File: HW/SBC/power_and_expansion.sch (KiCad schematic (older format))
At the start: 13 parts, among them J4 POWER IN, J5 Expansion Port, U11 LM7805

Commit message: Connected all relevant I/O select signals to expansion port.
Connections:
- net labels added: ~7FAX
- wire segments 71 -> 93
- no-connect marks 9 -> 8
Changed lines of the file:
@@
 	2425 2275 2425 2500
 Wire Wire Line
-	1900 2500 5625 2500
+	1900 2500 2425 2500
+Wire Wire Line
+	2425 2500 2825 2500
+Wire Wire Line
+	2825 2500 3225 2500
+Wire Wire Line
+	3225 2500 3550 2500
+Wire Wire Line
+	3550 2500 3800 2500
+Wire Wire Line
+	3800 2500 4050 2500
+Wire Wire Line
+	4050 2500 4300 2500
+Wire Wire Line
+	4300 2500 4550 2500
+Wire Wire Line
+	4550 2500 4800 2500
+Wire Wire Line
+	4800 2500 5050 2500
+Wire Wire Line
+	5050 2500 5300 2500
+Wire Wire Line
+	5300 2500 5625 2500
 Wire Wire Line
 	3225 2500 3225 2275
@@
 	1900 2125 1900 2500
 Wire Wire Line
-	3225 1650 5625 1650
+	3225 1650 3550 1650
+Wire Wire Line
+	3550 1650 3800 1650
+Wire Wire Line
+	3800 1650 4050 1650
+Wire Wire Line
+	4050 1650 4300 1650
+Wire Wire Line
+	4300 1650 4550 1650
+Wire Wire Line
+	4550 1650 4800 1650
+Wire Wire Line
+	4800 1650 5050 1650
+Wire Wire Line
+	5050 1650 5300 1650
+Wire Wire Line
+	5300 1650 5625 1650
 Wire Wire Line
 	3550 1750 3550 1650
@@
 	3350 3725 3350 3500
 Wire Wire Line
-	3350 3500 3850 3500
+	3350 3500 3600 3500
+Wire Wire Line
+	3600 3500 3850 3500
 Wire Wire Line
 	3850 3500 3850 3725
@@
 	3350 6125 3350 6325
 Wire Wire Line
-	3350 6325 3850 6325
+	3350 6325 3600 6325
+Wire Wire Line
+	3600 6325 3850 6325
 Wire Wire Line
 	3850 6325 3850 6125
@@
 Wire Wire Line
 	4250 6025 3850 5725
-NoConn ~ 3850 5825
 NoConn ~ 3850 5925
 NoConn ~ 3850 6025
@@
 	1    0    0    -1
 $EndComp
+Text GLabel 4250 6175 2    60   Input ~ 0
+~7FAX
+Wire Wire Line
+	4250 6175 3850 5825
 $EndSCHEMATC

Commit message: New MB design. Includes RTC. New IDE design.
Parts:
- removed U11: LM7805, TO_SOT_Packages_THT:TO-220_Vertical, symbol LM7805
- added U11: LM7805CT, TO_SOT_Packages_THT:TO-220_Vertical, symbol LM7805CT
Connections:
- wire segments 93 -> 72
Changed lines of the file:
@@
 $EndDescr
-$Comp
-L LM7805 U11
-U 1 1 58D5E978
-P 2825 1700
-F 0 "U11" H 2975 1504 50  0000 C CNN
-F 1 "LM7805" H 2825 1900 50  0000 C CNN
-F 2 "TO_SOT_Packages_THT:TO-220_Vertical" H 2825 1700 50  0001 C CNN
-F 3 "" H 2825 1700 50  0001 C CNN
-	1    2825 1700
-	1    0    0    -1
-$EndComp
 $Comp
 L CP1_Small C7
@@
 	2425 2275 2425 2500
 Wire Wire Line
-	1900 2500 2425 2500
-Wire Wire Line
-	2425 2500 2825 2500
-Wire Wire Line
-	2825 2500 3225 2500
-Wire Wire Line
-	3225 2500 3550 2500
-Wire Wire Line
-	3550 2500 3800 2500
-Wire Wire Line
-	3800 2500 4050 2500
-Wire Wire Line
-	4050 2500 4300 2500
-Wire Wire Line
-	4300 2500 4550 2500
-Wire Wire Line
-	4550 2500 4800 2500
-Wire Wire Line
-	4800 2500 5050 2500
-Wire Wire Line
-	5050 2500 5300 2500
-Wire Wire Line
-	5300 2500 5625 2500
+	1900 2500 5625 2500
 Wire Wire Line
 	3225 2500 3225 2275
@@
 	1900 2125 1900 2500
 Wire Wire Line
-	3225 1650 3550 1650
-Wire Wire Line
-	3550 1650 3800 1650
-Wire Wire Line
-	3800 1650 4050 1650
-Wire Wire Line
-	4050 1650 4300 1650
-Wire Wire Line
-	4300 1650 4550 1650
-Wire Wire Line
-	4550 1650 4800 1650
-Wire Wire Line
-	4800 1650 5050 1650
-Wire Wire Line
-	5050 1650 5300 1650
-Wire Wire Line
-	5300 1650 5625 1650
+	3225 1650 5625 1650
 Wire Wire Line
 	3550 1750 3550 1650
@@
 	3350 3725 3350 3500
 Wire Wire Line
-	3350 3500 3600 3500
-Wire Wire Line
-	3600 3500 3850 3500
+	3350 3500 3850 3500
 Wire Wire Line
 	3850 3500 3850 3725
@@
 	3350 6125 3350 6325
 Wire Wire Line
-	3350 6325 3600 6325
-Wire Wire Line
-	3600 6325 3850 6325
+	3350 6325 3850 6325
 Wire Wire Line
 	3850 6325 3850 6125
@@
 Wire Wire Line
 	4250 6175 3850 5825
+$Comp
+L LM7805CT U11
+U 1 1 58E10ED4
+P 2825 1700
+F 0 "U11" H 2625 1900 50  0000 C CNN
+F 1 "LM7805CT" H 2825 1900 50  0000 L CNN
+F 2 "TO_SOT_Packages_THT:TO-220_Vertical" H 2825 1800 50  0001 C CIN
+F 3 "" H 2825 1700 50  0001 C CNN
+	1    2825 1700
+	1    0    0    -1
+$EndComp
 $EndSCHEMATC

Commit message: Updates to pcb and monitor.
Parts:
- J5: footprint Pin_Headers:Pin_Header_Straight_2x25_Pitch2.54mm -> Connect:IDC_Header_Straight_50pins
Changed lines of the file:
@@
 $EndComp
 $Comp
-L VCC #PWR028
+L VCC #PWR029
 U 1 1 58D5EE10
 P 5625 1650
-F 0 "#PWR028" H 5625 1500 50  0001 C CNN
+F 0 "#PWR029" H 5625 1500 50  0001 C CNN
 F 1 "VCC" H 5625 1800 50  0000 C CNN
 F 2 "" H 5625 1650 50  0001 C CNN
@@
 F 0 "J5" H 3600 6225 50  0000 C CNN
 F 1 "Expansion Port" V 3600 4925 50  0000 C CNN
-F 2 "Pin_Headers:Pin_Header_Straight_2x25_Pitch2.54mm" H 3600 4175 50  0001 C CNN
+F 2 "Connect:IDC_Header_Straight_50pins" H 3600 4175 50  0001 C CNN
 F 3 "" H 3600 4175 50  0001 C CNN
 	1    3600 4925
@@
 	5300 1950 5300 2500
 $Comp
-L VCC #PWR029
+L VCC #PWR030
 U 1 1 58D7686C
 P 3600 3500
-F 0 "#PWR029" H 3600 3350 50  0001 C CNN
+F 0 "#PWR030" H 3600 3350 50  0001 C CNN
 F 1 "VCC" H 3600 3650 50  0000 C CNN
 F 2 "" H 3600 3500 50  0001 C CNN
@@
 Connection ~ 3600 3500
 $Comp
-L GND #PWR030
+L GND #PWR031
 U 1 1 58D76B4A
 P 3600 6325
-F 0 "#PWR030" H 3600 6075 50  0001 C CNN
+F 0 "#PWR031" H 3600 6075 50  0001 C CNN
 F 1 "GND" H 3600 6175 50  0000 C CNN
 F 2 "" H 3600 6325 50  0001 C CNN
@@
 Connection ~ 5300 2500
 $Comp
-L GND #PWR031
+L GND #PWR032
 U 1 1 58D85868
 P 5625 2500
-F 0 "#PWR031" H 5625 2250 50  0001 C CNN
+F 0 "#PWR032" H 5625 2250 50  0001 C CNN
 F 1 "GND" H 5625 2350 50  0000 C CNN
 F 2 "" H 5625 2500 50  0001 C CNN

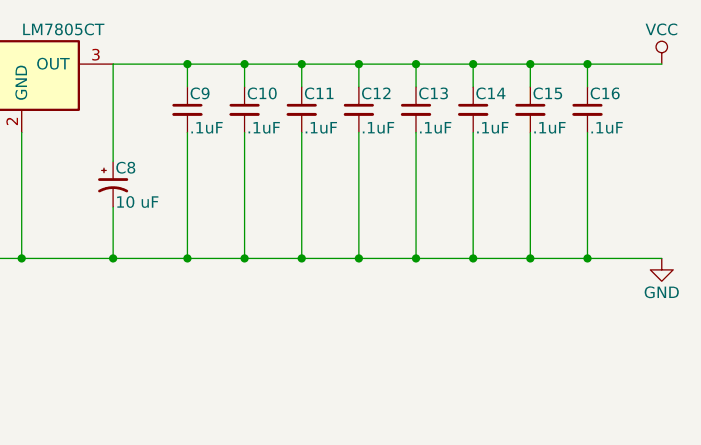
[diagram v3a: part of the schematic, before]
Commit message: Move dicoupling capacitators as close the chips as possible.
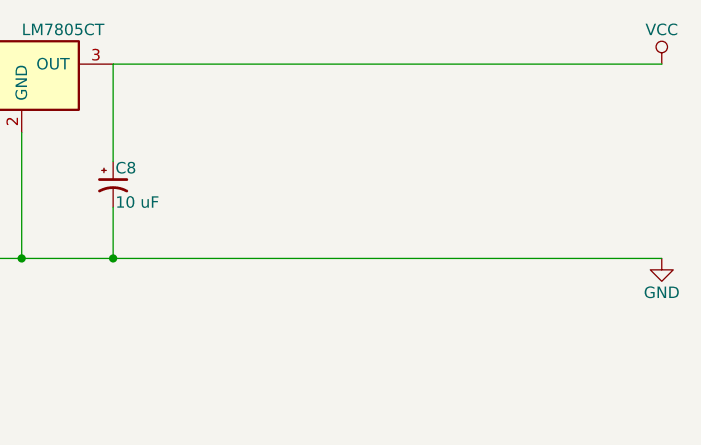
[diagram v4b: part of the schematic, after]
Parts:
- removed C10, C11, C12, C13, C14, C15, C16, C9: .1uF, Capacitors_ThroughHole:C_Disc_D3.8mm_W2.6mm_P2.50mm, symbol C_Small
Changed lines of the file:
@@
 +9V
-$Comp
-L C_Small C9
-U 1 1 58D74CC9
-P 3550 1850
-F 0 "C9" H 3560 1920 50  0000 L CNN
-F 1 ".1uF" H 3560 1770 50  0000 L CNN
-F 2 "Capacitors_ThroughHole:C_Disc_D3.8mm_W2.6mm_P2.50mm" H 3550 1850 50  0001 C CNN
-F 3 "" H 3550 1850 50  0001 C CNN
-	1    3550 1850
-	1    0    0    -1
-$EndComp
-$Comp
-L C_Small C10
-U 1 1 58D74D28
-P 3800 1850
-F 0 "C10" H 3810 1920 50  0000 L CNN
-F 1 ".1uF" H 3810 1770 50  0000 L CNN
-F 2 "Capacitors_ThroughHole:C_Disc_D3.8mm_W2.6mm_P2.50mm" H 3800 1850 50  0001 C CNN
-F 3 "" H 3800 1850 50  0001 C CNN
-	1    3800 1850
-	1    0    0    -1
-$EndComp
-$Comp
-L C_Small C11
-U 1 1 58D74D6D
-P 4050 1850
-F 0 "C11" H 4060 1920 50  0000 L CNN
-F 1 ".1uF" H 4060 1770 50  0000 L CNN
-F 2 "Capacitors_ThroughHole:C_Disc_D3.8mm_W2.6mm_P2.50mm" H 4050 1850 50  0001 C CNN
-F 3 "" H 4050 1850 50  0001 C CNN
-	1    4050 1850
-	1    0    0    -1
-$EndComp
-$Comp
-L C_Small C14
-U 1 1 58D74DA8
-P 4800 1850
-F 0 "C14" H 4810 1920 50  0000 L CNN
-F 1 ".1uF" H 4810 1770 50  0000 L CNN
-F 2 "Capacitors_ThroughHole:C_Disc_D3.8mm_W2.6mm_P2.50mm" H 4800 1850 50  0001 C CNN
-F 3 "" H 4800 1850 50  0001 C CNN
-	1    4800 1850
-	1    0    0    -1
-$EndComp
-$Comp
-L C_Small C12
-U 1 1 58D74DFB
-P 4300 1850
-F 0 "C12" H 4310 1920 50  0000 L CNN
-F 1 ".1uF" H 4310 1770 50  0000 L CNN
-F 2 "Capacitors_ThroughHole:C_Disc_D3.8mm_W2.6mm_P2.50mm" H 4300 1850 50  0001 C CNN
-F 3 "" H 4300 1850 50  0001 C CNN
-	1    4300 1850
-	1    0    0    -1
-$EndComp
-$Comp
-L C_Small C13
-U 1 1 58D74E20
-P 4550 1850
-F 0 "C13" H 4560 1920 50  0000 L CNN
-F 1 ".1uF" H 4560 1770 50  0000 L CNN
-F 2 "Capacitors_ThroughHole:C_Disc_D3.8mm_W2.6mm_P2.50mm" H 4550 1850 50  0001 C CNN
-F 3 "" H 4550 1850 50  0001 C CNN
-	1    4550 1850
-	1    0    0    -1
-$EndComp
-$Comp
-L C_Small C16
-U 1 1 58D74E77
-P 5300 1850
-F 0 "C16" H 5310 1920 50  0000 L CNN
-F 1 ".1uF" H 5310 1770 50  0000 L CNN
-F 2 "Capacitors_ThroughHole:C_Disc_D3.8mm_W2.6mm_P2.50mm" H 5300 1850 50  0001 C CNN
-F 3 "" H 5300 1850 50  0001 C CNN
-	1    5300 1850
-	1    0    0    -1
-$EndComp
-$Comp
-L C_Small C15
-U 1 1 58D74EA0
-P 5050 1850
-F 0 "C15" H 5060 1920 50  0000 L CNN
-F 1 ".1uF" H 5060 1770 50  0000 L CNN
-F 2 "Capacitors_ThroughHole:C_Disc_D3.8mm_W2.6mm_P2.50mm" H 5050 1850 50  0001 C CNN
-F 3 "" H 5050 1850 50  0001 C CNN
-	1    5050 1850
-	1    0    0    -1
-$EndComp
 $Comp
 L CONN_02X25 J5
@@
 Wire Wire Line
 	3225 1650 5625 1650
-Wire Wire Line
-	3550 1750 3550 1650
-Connection ~ 3550 1650
-Wire Wire Line
-	3550 1950 3550 2500
-Wire Wire Line
-	3800 1750 3800 1650
-Connection ~ 3800 1650
-Wire Wire Line
-	3800 1950 3800 2500
-Wire Wire Line
-	4050 1750 4050 1650
-Connection ~ 4050 1650
-Wire Wire Line
-	4050 1950 4050 2500
-Wire Wire Line
-	4300 1750 4300 1650
-Connection ~ 4300 1650
-Wire Wire Line
-	4300 1950 4300 2500
-Wire Wire Line
-	4550 1750 4550 1650
-Connection ~ 4550 1650
-Wire Wire Line
-	4550 1950 4550 2500
-Wire Wire Line
-	4800 1750 4800 1650
-Connection ~ 4800 1650
-Wire Wire Line
-	4800 1950 4800 2500
-Wire Wire Line
-	5050 1750 5050 1650
-Connection ~ 5050 1650
-Wire Wire Line
-	5050 1950 5050 2500
-Wire Wire Line
-	5300 1750 5300 1650
-Connection ~ 5300 1650
-Wire Wire Line
-	5300 1950 5300 2500
 $Comp
 L VCC #PWR030
@@
 NoConn ~ 3850 6025
 Connection ~ 3225 2500
-Connection ~ 3550 2500
-Connection ~ 3800 2500
-Connection ~ 4050 2500
-Connection ~ 4300 2500
-Connection ~ 4550 2500
-Connection ~ 4800 2500
-Connection ~ 5050 2500
-Connection ~ 5300 2500
 $Comp
 L GND #PWR032

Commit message: New board layout. WIP
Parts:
- added MK1, MK2, MK3, MK4: Mounting_Hole, Mounting_Holes:MountingHole_3.2mm_M3_Pad, symbol Mounting_Hole
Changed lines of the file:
@@
 $EndComp
 $Comp
-L VCC #PWR029
+L VCC #PWR025
 U 1 1 58D5EE10
 P 5625 1650
-F 0 "#PWR029" H 5625 1500 50  0001 C CNN
+F 0 "#PWR025" H 5625 1500 50  0001 C CNN
 F 1 "VCC" H 5625 1800 50  0000 C CNN
 F 2 "" H 5625 1650 50  0001 C CNN
@@
 	3225 1650 5625 1650
 $Comp
-L VCC #PWR030
+L VCC #PWR026
 U 1 1 58D7686C
 P 3600 3500
-F 0 "#PWR030" H 3600 3350 50  0001 C CNN
+F 0 "#PWR026" H 3600 3350 50  0001 C CNN
 F 1 "VCC" H 3600 3650 50  0000 C CNN
 F 2 "" H 3600 3500 50  0001 C CNN
@@
 Connection ~ 3600 3500
 $Comp
-L GND #PWR031
+L GND #PWR027
 U 1 1 58D76B4A
 P 3600 6325
-F 0 "#PWR031" H 3600 6075 50  0001 C CNN
+F 0 "#PWR027" H 3600 6075 50  0001 C CNN
 F 1 "GND" H 3600 6175 50  0000 C CNN
 F 2 "" H 3600 6325 50  0001 C CNN
@@
 Connection ~ 3225 2500
 $Comp
-L GND #PWR032
+L GND #PWR028
 U 1 1 58D85868
 P 5625 2500
-F 0 "#PWR032" H 5625 2250 50  0001 C CNN
+F 0 "#PWR028" H 5625 2250 50  0001 C CNN
 F 1 "GND" H 5625 2350 50  0000 C CNN
 F 2 "" H 5625 2500 50  0001 C CNN
@@
 	1    0    0    -1
 $EndComp
+$Comp
+L Mounting_Hole MK1
+U 1 1 59149E0C
+P 6050 3325
+F 0 "MK1" H 6050 3525 50  0000 C CNN
+F 1 "Mounting_Hole" H 6050 3450 50  0000 C CNN
+F 2 "Mounting_Holes:MountingHole_3.2mm_M3_Pad" H 6050 3325 50  0001 C CNN
+F 3 "" H 6050 3325 50  0001 C CNN
+	1    6050 3325
+	1    0    0    -1
+$EndComp
+$Comp
+L Mounting_Hole MK2
+U 1 1 59149E41
+P 6050 3725
+F 0 "MK2" H 6050 3925 50  0000 C CNN
+F 1 "Mounting_Hole" H 6050 3850 50  0000 C CNN
+F 2 "Mounting_Holes:MountingHole_3.2mm_M3_Pad" H 6050 3725 50  0001 C CNN
+F 3 "" H 6050 3725 50  0001 C CNN
+	1    6050 3725
+	1    0    0    -1
+$EndComp
+$Comp
+L Mounting_Hole MK3
+U 1 1 59149E60
+P 6750 3300
+F 0 "MK3" H 6750 3500 50  0000 C CNN
+F 1 "Mounting_Hole" H 6750 3425 50  0000 C CNN
+F 2 "Mounting_Holes:MountingHole_3.2mm_M3_Pad" H 6750 3300 50  0001 C CNN
+F 3 "" H 6750 3300 50  0001 C CNN
+	1    6750 3300
+	1    0    0    -1
+$EndComp
+$Comp
+L Mounting_Hole MK4
+U 1 1 59149E83
+P 6750 3725
+F 0 "MK4" H 6750 3925 50  0000 C CNN
+F 1 "Mounting_Hole" H 6750 3850 50  0000 C CNN
+F 2 "Mounting_Holes:MountingHole_3.2mm_M3_Pad" H 6750 3725 50  0001 C CNN
+F 3 "" H 6750 3725 50  0001 C CNN
+	1    6750 3725
+	1    0    0    -1
+$EndComp
